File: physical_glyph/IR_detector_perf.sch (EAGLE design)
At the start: 19 parts, among them IC1 7805T, T1 BP103, U1 MCP6004-I/P, U2 LM339PWR

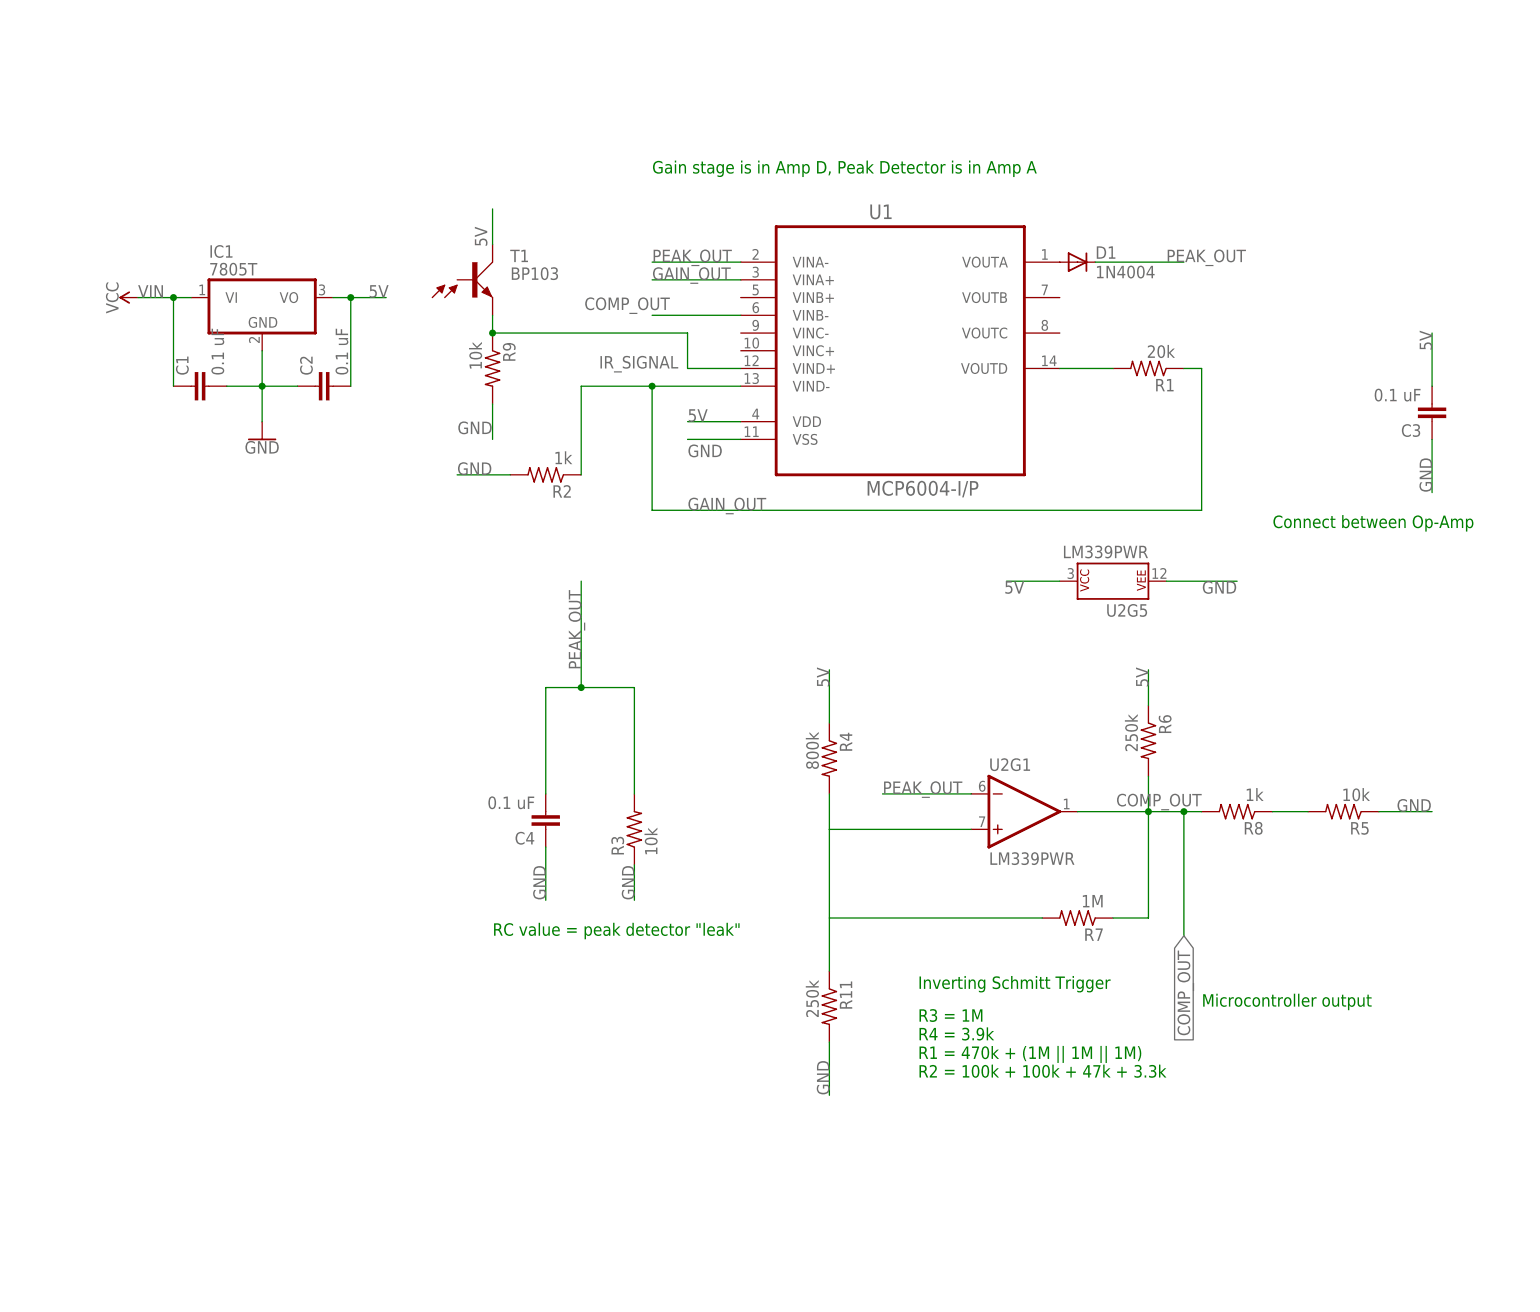
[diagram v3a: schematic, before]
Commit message: Change hystersis bounds and peak detector
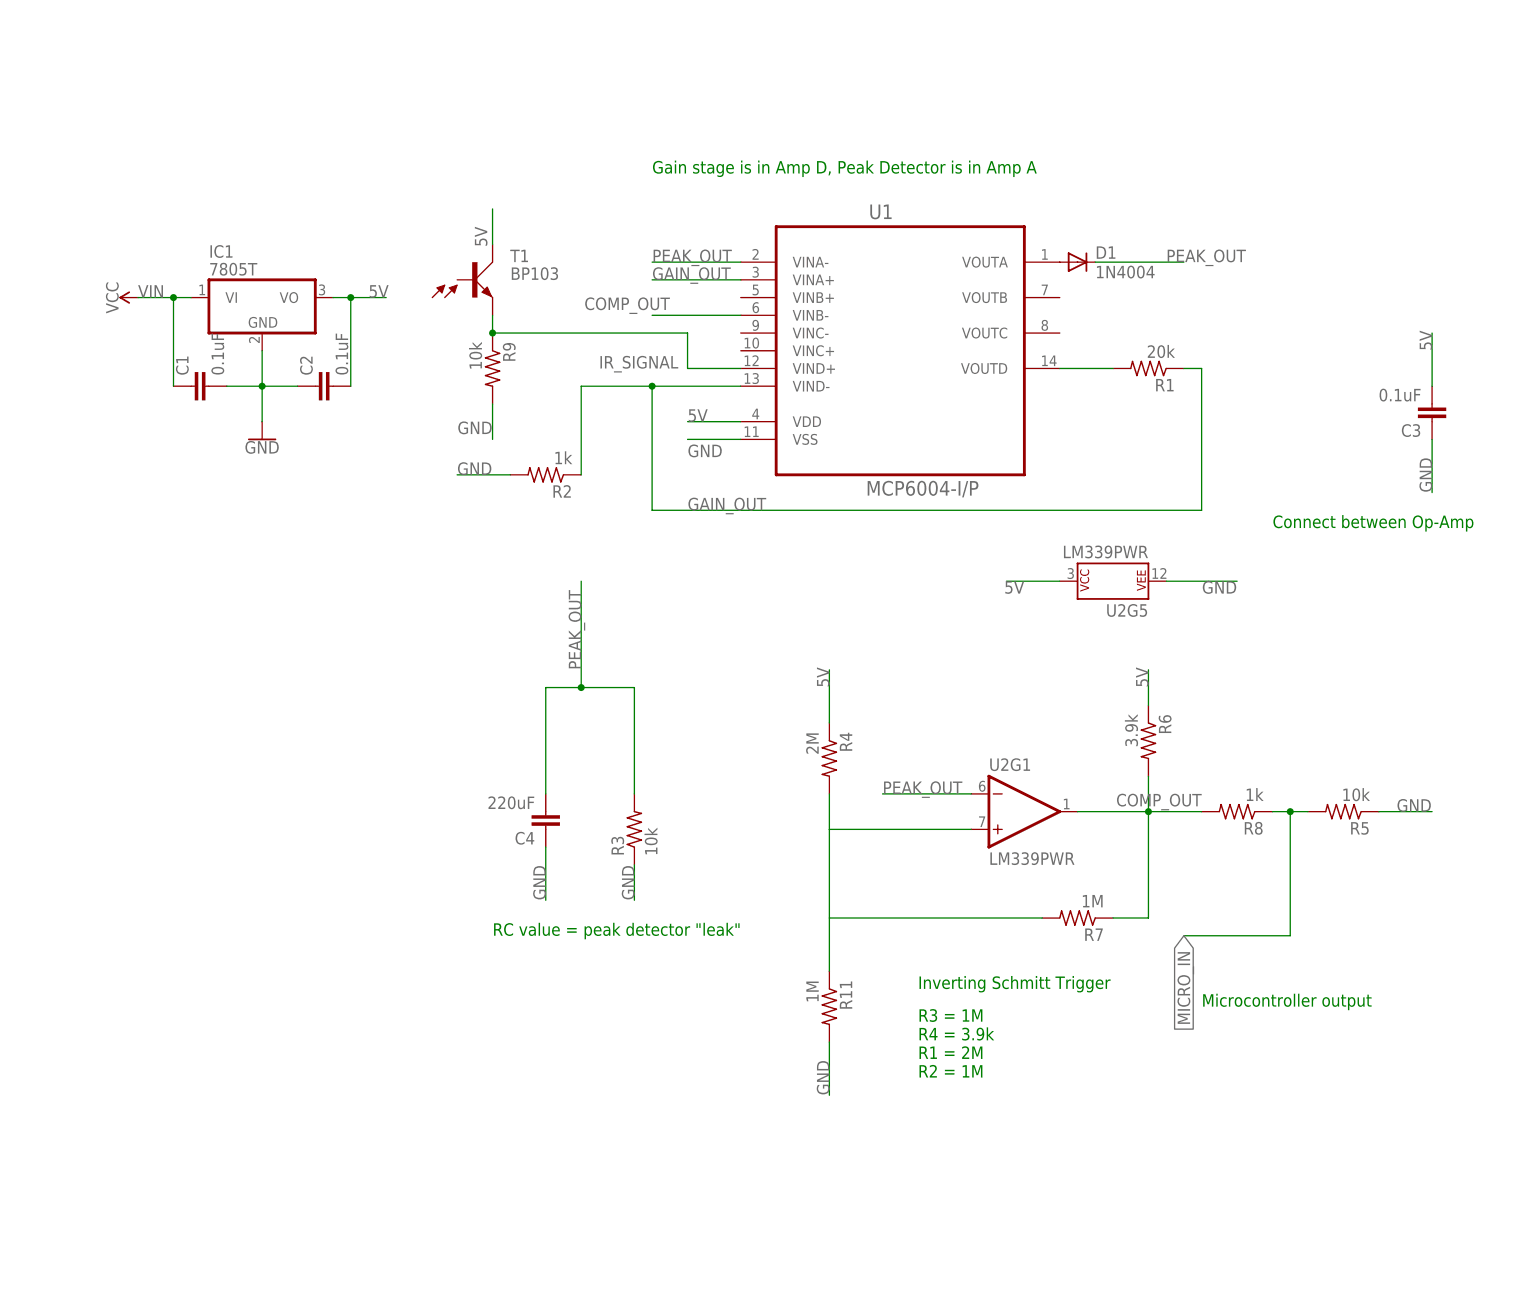
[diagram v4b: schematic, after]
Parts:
- C1, C2, C3: value 0.1 uF -> 0.1uF
- C4: value 0.1 uF -> 220uF
- R11: value 250k -> 1M
- R4: value 800k -> 2M
- R6: value 250k -> 3.9k
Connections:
- net N$1 renamed MICRO_IN
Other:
- note added: "R3 = 1M R4 = 3.9k R1 = 2M R2 = 1M"
- note removed: "R3 = 1M R4 = 3.9k R1 = 470k + (1M || 1M || 1M) R2 = 100k + 100k + 47k + 3.3k"
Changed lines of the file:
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@@
 <part name="U1" library="Microchip_By_element14_Batch_1" deviceset="MCP6004-I/P" device=""/>
 <part name="D1" library="diode" library_urn="urn:adsk.eagle:library:210" deviceset="1N4004" device="" package3d_urn="urn:adsk.eagle:package:43336/1"/>
-<part name="C1" library="resistor" library_urn="urn:adsk.eagle:library:348" deviceset="C-EU" device="025-024X044" package3d_urn="urn:adsk.eagle:package:26149/1" value="0.1 uF"/>
-<part name="C2" library="resistor" library_urn="urn:adsk.eagle:library:348" deviceset="C-EU" device="025-024X044" package3d_urn="urn:adsk.eagle:package:26149/1" value="0.1 uF"/>
+<part name="C1" library="resistor" library_urn="urn:adsk.eagle:library:348" deviceset="C-EU" device="025-024X044" package3d_urn="urn:adsk.eagle:package:26149/1" value="0.1uF"/>
+<part name="C2" library="resistor" library_urn="urn:adsk.eagle:library:348" deviceset="C-EU" device="025-024X044" package3d_urn="urn:adsk.eagle:package:26149/1" value="0.1uF"/>
 <part name="T1" library="opto-trans-siemens" library_urn="urn:adsk.eagle:library:317" deviceset="BP103" device="" package3d_urn="urn:adsk.eagle:package:21787/1"/>
 <part name="R1" library="rcl" library_urn="urn:adsk.eagle:library:334" deviceset="R-US_" device="0204/2V" package3d_urn="urn:adsk.eagle:package:23495/1" value="20k"/>
 <part name="R2" library="rcl" library_urn="urn:adsk.eagle:library:334" deviceset="R-US_" device="0204/2V" package3d_urn="urn:adsk.eagle:package:23495/1" value="1k"/>
 <part name="R3" library="rcl" library_urn="urn:adsk.eagle:library:334" deviceset="R-US_" device="0204/2V" package3d_urn="urn:adsk.eagle:package:23495/1" value="10k"/>
-<part name="R4" library="rcl" library_urn="urn:adsk.eagle:library:334" deviceset="R-US_" device="0204/2V" package3d_urn="urn:adsk.eagle:package:23495/1" value="800k"/>
+<part name="R4" library="rcl" library_urn="urn:adsk.eagle:library:334" deviceset="R-US_" device="0204/2V" package3d_urn="urn:adsk.eagle:package:23495/1" value="2M"/>
 <part name="R7" library="rcl" library_urn="urn:adsk.eagle:library:334" deviceset="R-US_" device="0204/2V" package3d_urn="urn:adsk.eagle:package:23495/1" value="1M"/>
-<part name="R11" library="rcl" library_urn="urn:adsk.eagle:library:334" deviceset="R-US_" device="0204/2V" package3d_urn="urn:adsk.eagle:package:23495/1" value="250k"/>
-<part name="C3" library="resistor" library_urn="urn:adsk.eagle:library:348" deviceset="C-EU" device="025-024X044" package3d_urn="urn:adsk.eagle:package:26149/1" value="0.1 uF"/>
-<part name="C4" library="resistor" library_urn="urn:adsk.eagle:library:348" deviceset="C-EU" device="025-024X044" package3d_urn="urn:adsk.eagle:package:26149/1" value="0.1 uF"/>
+<part name="R11" library="rcl" library_urn="urn:adsk.eagle:library:334" deviceset="R-US_" device="0204/2V" package3d_urn="urn:adsk.eagle:package:23495/1" value="1M"/>
+<part name="C3" library="resistor" library_urn="urn:adsk.eagle:library:348" deviceset="C-EU" device="025-024X044" package3d_urn="urn:adsk.eagle:package:26149/1" value="0.1uF"/>
+<part name="C4" library="resistor" library_urn="urn:adsk.eagle:library:348" deviceset="C-EU" device="025-024X044" package3d_urn="urn:adsk.eagle:package:26149/1" value="220uF"/>
 <part name="U2" library="SparkFun-IC-Amplifiers" deviceset="LM339" device="" value="LM339PWR"/>
-<part name="R6" library="rcl" library_urn="urn:adsk.eagle:library:334" deviceset="R-US_" device="0204/2V" package3d_urn="urn:adsk.eagle:package:23495/1" value="250k"/>
+<part name="R6" library="rcl" library_urn="urn:adsk.eagle:library:334" deviceset="R-US_" device="0204/2V" package3d_urn="urn:adsk.eagle:package:23495/1" value="3.9k"/>
 <part name="R5" library="rcl" library_urn="urn:adsk.eagle:library:334" deviceset="R-US_" device="0204/2V" package3d_urn="urn:adsk.eagle:package:23495/1" value="10k"/>
 <part name="R8" library="rcl" library_urn="urn:adsk.eagle:library:334" deviceset="R-US_" device="0204/2V" package3d_urn="urn:adsk.eagle:package:23495/1" value="1k"/>
@@
 <text x="78.74" y="-27.94" size="1.778" layer="91">R3 = 1M
 R4 = 3.9k
-R1 = 470k + (1M || 1M || 1M)
-R2 = 100k + 100k + 47k + 3.3k</text>
+R1 = 2M
+R2 = 1M</text>
 <text x="17.78" y="-7.62" size="1.778" layer="91">RC value = peak detector "leak"</text>
 <text x="78.74" y="-15.24" size="1.778" layer="91">Inverting Schmitt Trigger</text>
@@
 </segment>
 <segment>
-<label x="116.84" y="-7.62" size="1.778" layer="95" rot="R270" xref="yes"/>
-<wire x1="116.84" y1="10.16" x2="116.84" y2="-7.62" width="0.1524" layer="91"/>
 <pinref part="U2" gate="G1" pin="OUT"/>
 <label x="119.38" y="12.7" size="1.778" layer="95" rot="R180"/>
 <wire x1="101.6" y1="10.16" x2="111.76" y2="10.16" width="0.1524" layer="91"/>
 <pinref part="R7" gate="G$1" pin="1"/>
-<wire x1="111.76" y1="10.16" x2="116.84" y2="10.16" width="0.1524" layer="91"/>
-<wire x1="116.84" y1="10.16" x2="119.38" y2="10.16" width="0.1524" layer="91"/>
+<wire x1="111.76" y1="10.16" x2="119.38" y2="10.16" width="0.1524" layer="91"/>
 <wire x1="106.68" y1="-5.08" x2="111.76" y2="-5.08" width="0.1524" layer="91"/>
 <wire x1="111.76" y1="-5.08" x2="111.76" y2="10.16" width="0.1524" layer="91"/>
@@
 <wire x1="111.76" y1="15.24" x2="111.76" y2="10.16" width="0.1524" layer="91"/>
 <pinref part="R8" gate="G$1" pin="2"/>
-<junction x="116.84" y="10.16"/>
 </segment>
 </net>
@@
 </segment>
 </net>
-<net name="N$1" class="0">
+<net name="MICRO_IN" class="0">
 <segment>
 <pinref part="R8" gate="G$1" pin="1"/>
 <pinref part="R5" gate="G$1" pin="2"/>
-<wire x1="129.54" y1="10.16" x2="134.62" y2="10.16" width="0.1524" layer="91"/>
-</segment>
-</net>
+<wire x1="129.54" y1="10.16" x2="132.08" y2="10.16" width="0.1524" layer="91"/>
+<wire x1="132.08" y1="10.16" x2="134.62" y2="10.16" width="0.1524" layer="91"/>
+<wire x1="132.08" y1="10.16" x2="132.08" y2="-7.62" width="0.1524" layer="91"/>
+<junction x="132.08" y="10.16"/>
+<wire x1="132.08" y1="-7.62" x2="116.84" y2="-7.62" width="0.1524" layer="91"/>
+<label x="116.84" y="-7.62" size="1.778" layer="95" rot="R270" xref="yes"/>
+</segment>
+</net>
